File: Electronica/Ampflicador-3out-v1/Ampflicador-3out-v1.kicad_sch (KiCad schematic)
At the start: 20 parts, among them U1 LM386

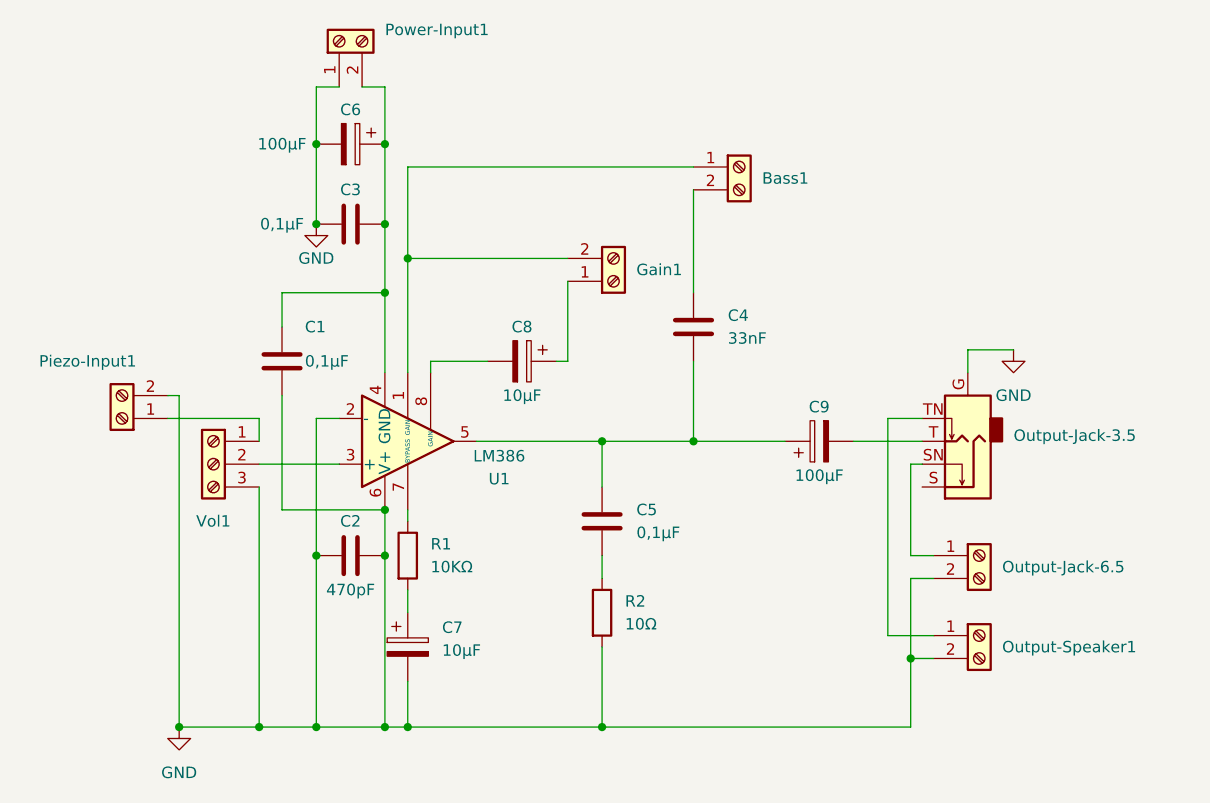
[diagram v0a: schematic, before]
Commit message: Amp v1 sin plano de masa
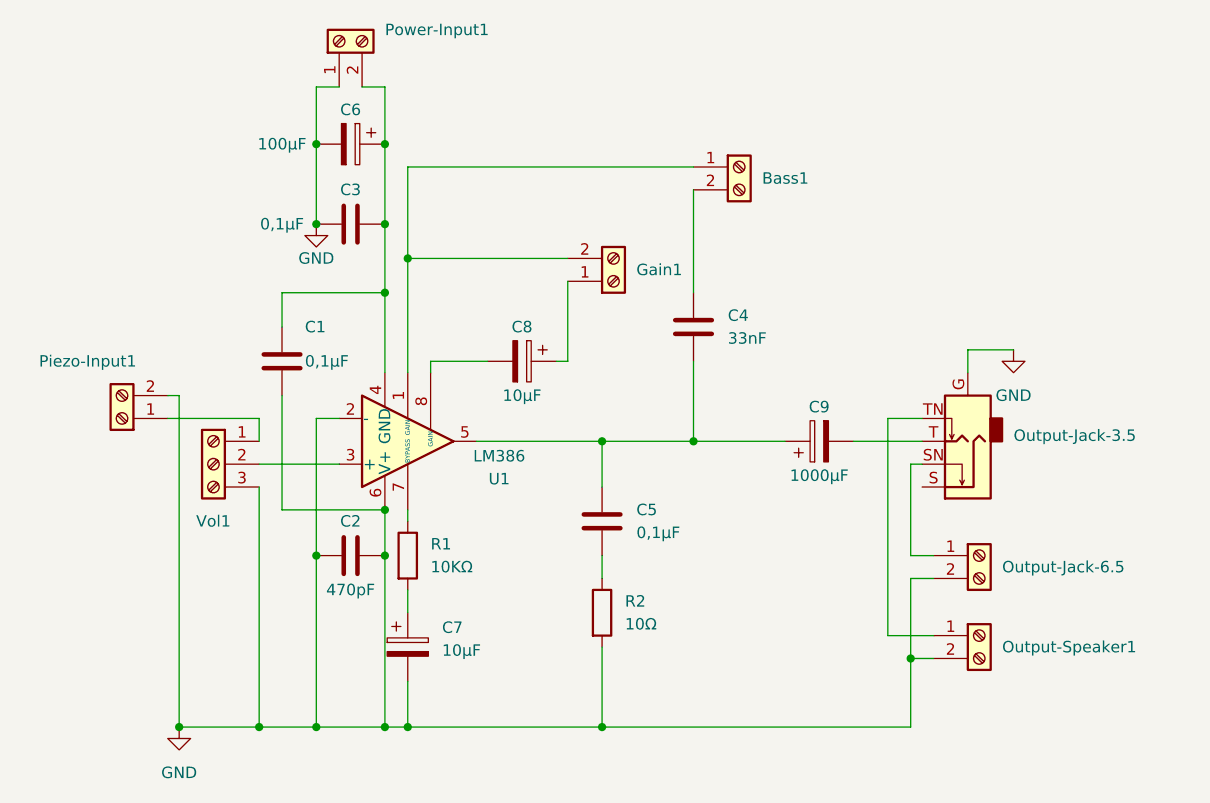
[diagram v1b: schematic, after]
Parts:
- C1, C2, C3, C4, C5: footprint Capacitor_THT:C_Axial_L3.8mm_D2.6mm_P7.50mm_Horizontal -> Capacitor_THT:C_Disc_D3.0mm_W1.6mm_P2.50mm
- C6: footprint Capacitor_THT:CP_Axial_L10.0mm_D4.5mm_P15.00mm_Horizontal -> Capacitor_THT:CP_Radial_D6.3mm_P2.50mm
- C7, C8: footprint Capacitor_THT:CP_Axial_L10.0mm_D4.5mm_P15.00mm_Horizontal -> Capacitor_THT:CP_Radial_D4.0mm_P2.00mm
- C9: value 100µF -> 1000µF; footprint Capacitor_THT:CP_Axial_L10.0mm_D4.5mm_P15.00mm_Horizontal -> Capacitor_THT:CP_Radial_Tantal_D9.0mm_P5.00mm
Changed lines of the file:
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@@
       (effects (font (size 1.27 1.27)) (justify left))
     )
-    (property "Footprint" "Capacitor_THT:C_Axial_L3.8mm_D2.6mm_P7.50mm_Horizontal" (at 141.9352 109.22 0)
+    (property "Footprint" "Capacitor_THT:C_Disc_D3.0mm_W1.6mm_P2.50mm" (at 141.9352 109.22 0)
       (effects (font (size 1.27 1.27)) hide)
     )
@@
       (effects (font (size 1.27 1.27)))
     )
-    (property "Footprint" "Capacitor_THT:C_Axial_L3.8mm_D2.6mm_P7.50mm_Horizontal" (at 109.22 110.1852 0)
+    (property "Footprint" "Capacitor_THT:C_Disc_D3.0mm_W1.6mm_P2.50mm" (at 109.22 110.1852 0)
       (effects (font (size 1.27 1.27)) hide)
     )
@@
       (effects (font (size 1.27 1.27)) (justify left))
     )
-    (property "Footprint" "Capacitor_THT:C_Axial_L3.8mm_D2.6mm_P7.50mm_Horizontal" (at 152.0952 87.63 0)
+    (property "Footprint" "Capacitor_THT:C_Disc_D3.0mm_W1.6mm_P2.50mm" (at 152.0952 87.63 0)
       (effects (font (size 1.27 1.27)) hide)
     )
@@
       (effects (font (size 1.27 1.27)))
     )
-    (property "Footprint" "Capacitor_THT:CP_Axial_L10.0mm_D4.5mm_P15.00mm_Horizontal" (at 128.27 88.5952 0)
+    (property "Footprint" "Capacitor_THT:CP_Radial_D4.0mm_P2.00mm" (at 128.27 88.5952 0)
       (effects (font (size 1.27 1.27)) hide)
     )
@@
       (effects (font (size 1.27 1.27)))
     )
-    (property "Footprint" "Capacitor_THT:CP_Axial_L10.0mm_D4.5mm_P15.00mm_Horizontal" (at 109.22 64.4652 0)
+    (property "Footprint" "Capacitor_THT:CP_Radial_D6.3mm_P2.50mm" (at 109.22 64.4652 0)
       (effects (font (size 1.27 1.27)) hide)
     )
@@
       (effects (font (size 1.27 1.27)))
     )
-    (property "Footprint" "Capacitor_THT:C_Axial_L3.8mm_D2.6mm_P7.50mm_Horizontal" (at 116.84 71.4248 0)
+    (property "Footprint" "Capacitor_THT:C_Disc_D3.0mm_W1.6mm_P2.50mm" (at 116.84 71.4248 0)
       (effects (font (size 1.27 1.27)) hide)
     )
@@
       (effects (font (size 1.27 1.27)))
     )
-    (property "Value" "100µF" (at 165.1 100.33 90)
-      (effects (font (size 1.27 1.27)))
-    )
-    (property "Footprint" "Capacitor_THT:CP_Axial_L10.0mm_D4.5mm_P15.00mm_Horizontal" (at 168.91 95.5548 0)
+    (property "Value" "1000µF" (at 165.1 100.33 90)
+      (effects (font (size 1.27 1.27)))
+    )
+    (property "Footprint" "Capacitor_THT:CP_Radial_Tantal_D9.0mm_P5.00mm" (at 168.91 95.5548 0)
       (effects (font (size 1.27 1.27)) hide)
     )
@@
       (effects (font (size 1.27 1.27)) (justify left))
     )
-    (property "Footprint" "Capacitor_THT:CP_Axial_L10.0mm_D4.5mm_P15.00mm_Horizontal" (at 120.3452 123.19 0)
+    (property "Footprint" "Capacitor_THT:CP_Radial_D4.0mm_P2.00mm" (at 120.3452 123.19 0)
       (effects (font (size 1.27 1.27)) hide)
     )
@@
       (effects (font (size 1.27 1.27)) (justify left))
     )
-    (property "Footprint" "Capacitor_THT:C_Axial_L3.8mm_D2.6mm_P7.50mm_Horizontal" (at 106.3752 91.44 0)
-      (effects (font (size 1.27 1.27)) hide)
-    )
+    (property "Footprint" "Capacitor_THT:C_Disc_D3.0mm_W1.6mm_P2.50mm" (at 106.3752 91.44 0)
+      (effects (font (size 1.27 1.27)) hide)
+    )

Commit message: Amp V1
Plano de masa
Cambiar pads de los cap. de 10microF
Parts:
- C1, C2, C3, C4, C5: footprint Capacitor_THT:C_Disc_D3.0mm_W1.6mm_P2.50mm -> Capacitor_THT:C_Disc_D5.0mm_W2.5mm_P2.50mm
- C6: footprint Capacitor_THT:CP_Radial_D6.3mm_P2.50mm -> Capacitor_THT:CP_Radial_D5.0mm_P2.50mm
- C7, C8: footprint Capacitor_THT:CP_Radial_D4.0mm_P2.00mm -> Capacitor_THT:CP_Radial_D4.0mm_P1.50mm
